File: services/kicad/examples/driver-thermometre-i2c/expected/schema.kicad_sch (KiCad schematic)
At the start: 10 parts, among them J1 CONN_5V_GND_SDA_SCL, U1 AMS1117-3.3

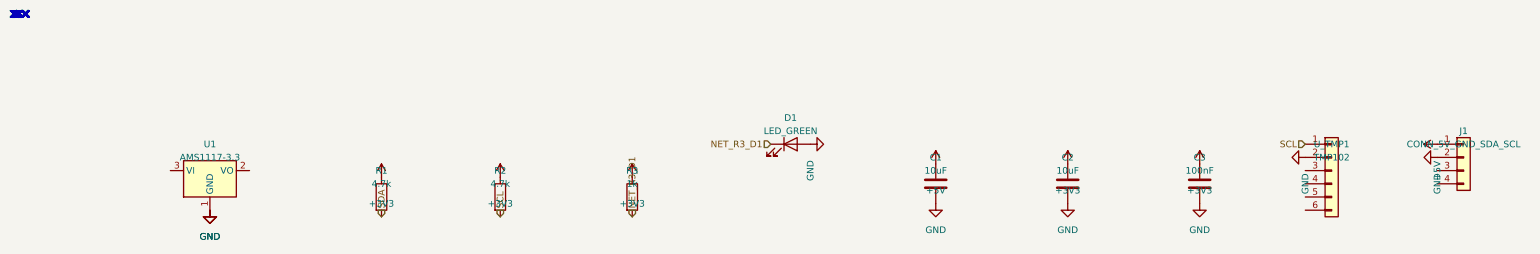
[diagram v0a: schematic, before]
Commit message: fix(agents): l'enrichissement ne reecrit plus un footprint deja qualifie ; exemple driver-thermometre-i2c sur le contrat durci
`quickLookup('J1', …)` rend un PinHeader 1x02 pour tout connecteur, quel que
soit l'indice : un footprint complet et juste (PinHeader_1x04) etait reecrit
en 1x02 dans l'etat publie et la BOM — le board, lui, gardait le bon. Un
footprint `Lib:Nom` ne se cherche plus.

Meme phrase rejouee sur le contrat durci (run 537dc8a5) : SDA passe de 1 a
3 broches, SCL de 2 a 3, 100 % route, 0 erreur, 198 s. README avant/apres.

Co-Authored-By: Claude Fable 5.1 <noreply@anthropic.com>
Claude-Session: https://claude.ai/code/session_01TnMqm4La2CxQHHB5K8aSSV
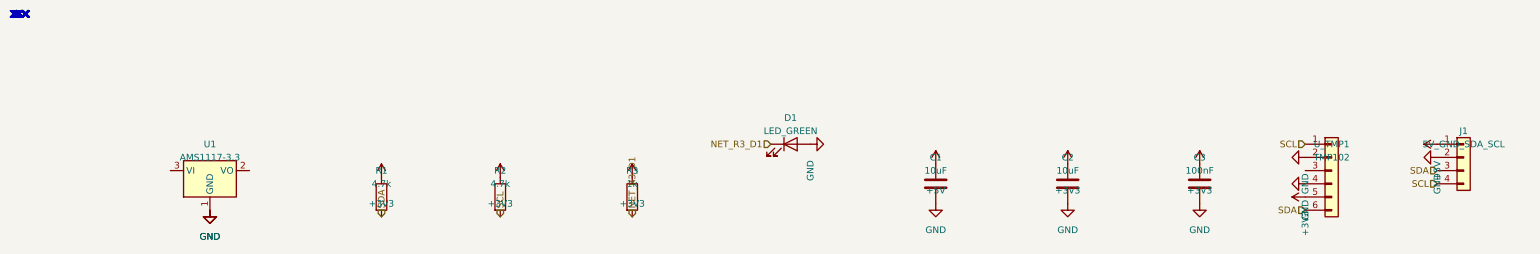
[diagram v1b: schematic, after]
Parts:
- J1: value CONN_5V_GND_SDA_SCL -> 5V_GND_SDA_SCL
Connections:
- net +3V3: now also U_TMP1.5 (Pin_5)
- net GND: now also U_TMP1.4 (Pin_4)
- net SCL: now also J1.4 (Pin_4)
- net SDA: now also J1.3 (Pin_3), U_TMP1.6 (Pin_6)
- no-connect marks 39 -> 33
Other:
- title: 2be02059-834b-4858-8c30-65f833ef493a -> 27ced4b4-4904-46c2-9a70-1466fee604bc
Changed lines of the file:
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@@
 	(paper "A4")
 	(title_block
-		(title "2be02059-834b-4858-8c30-65f833ef493a")
+		(title "27ced4b4-4904-46c2-9a70-1466fee604bc")
 		(date "")
 		(rev "")
@@
 			)
 		)
-		(property "Value" "CONN_5V_GND_SDA_SCL"
+		(property "Value" "5V_GND_SDA_SCL"
 			(at 279.4 25.4 0)
 			(effects
@@
 		(instances
 			(project "project"
-				(path "/40d6248a-0bee-4247-bdab-fa8b0e9ebeb3" (reference "J1") (unit 1)
+				(path "/6469032a-9a26-486a-b3b8-bd033d9a65b8" (reference "J1") (unit 1)
 				)
 			)
@@
 		(instances
 			(project "project"
-				(path "/40d6248a-0bee-4247-bdab-fa8b0e9ebeb3" (reference "U1") (unit 1)
+				(path "/6469032a-9a26-486a-b3b8-bd033d9a65b8" (reference "U1") (unit 1)
 				)
 			)
@@
 		(instances
 			(project "project"
-				(path "/40d6248a-0bee-4247-bdab-fa8b0e9ebeb3" (reference "C1") (unit 1)
+				(path "/6469032a-9a26-486a-b3b8-bd033d9a65b8" (reference "C1") (unit 1)
 				)
 			)
@@
 		(instances
 			(project "project"
-				(path "/40d6248a-0bee-4247-bdab-fa8b0e9ebeb3" (reference "C2") (unit 1)
+				(path "/6469032a-9a26-486a-b3b8-bd033d9a65b8" (reference "C2") (unit 1)
 				)
 			)
@@
 		(instances
 			(project "project"
-				(path "/40d6248a-0bee-4247-bdab-fa8b0e9ebeb3" (reference "C3") (unit 1)
+				(path "/6469032a-9a26-486a-b3b8-bd033d9a65b8" (reference "C3") (unit 1)
 				)
 			)
@@
 		(instances
 			(project "project"
-				(path "/40d6248a-0bee-4247-bdab-fa8b0e9ebeb3" (reference "U_TMP1") (unit 1)
+				(path "/6469032a-9a26-486a-b3b8-bd033d9a65b8" (reference "U_TMP1") (unit 1)
 				)
 			)
@@
 		(instances
 			(project "project"
-				(path "/40d6248a-0bee-4247-bdab-fa8b0e9ebeb3" (reference "R1") (unit 1)
+				(path "/6469032a-9a26-486a-b3b8-bd033d9a65b8" (reference "R1") (unit 1)
 				)
 			)
@@
 		(instances
 			(project "project"
-				(path "/40d6248a-0bee-4247-bdab-fa8b0e9ebeb3" (reference "R2") (unit 1)
+				(path "/6469032a-9a26-486a-b3b8-bd033d9a65b8" (reference "R2") (unit 1)
 				)
 			)
@@
 		(instances
 			(project "project"
-				(path "/40d6248a-0bee-4247-bdab-fa8b0e9ebeb3" (reference "R3") (unit 1)
+				(path "/6469032a-9a26-486a-b3b8-bd033d9a65b8" (reference "R3") (unit 1)
 				)
 			)
@@
 		(instances
 			(project "project"
-				(path "/40d6248a-0bee-4247-bdab-fa8b0e9ebeb3" (reference "D1") (unit 1)
+				(path "/6469032a-9a26-486a-b3b8-bd033d9a65b8" (reference "D1") (unit 1)
 				)
 			)
@@
 		(instances
 			(project "project"
-				(path "/40d6248a-0bee-4247-bdab-fa8b0e9ebeb3" (reference "#PWR001") (unit 1)
+				(path "/6469032a-9a26-486a-b3b8-bd033d9a65b8" (reference "#PWR001") (unit 1)
 				)
 			)
@@
 		(instances
 			(project "project"
-				(path "/40d6248a-0bee-4247-bdab-fa8b0e9ebeb3" (reference "#PWR002") (unit 1)
+				(path "/6469032a-9a26-486a-b3b8-bd033d9a65b8" (reference "#PWR002") (unit 1)
 				)
 			)
@@
 		(instances
 			(project "project"
-				(path "/40d6248a-0bee-4247-bdab-fa8b0e9ebeb3" (reference "#PWR003") (unit 1)
+				(path "/6469032a-9a26-486a-b3b8-bd033d9a65b8" (reference "#PWR003") (unit 1)
 				)
 			)
@@
 		(instances
 			(project "project"
-				(path "/40d6248a-0bee-4247-bdab-fa8b0e9ebeb3" (reference "#PWR004") (unit 1)
+				(path "/6469032a-9a26-486a-b3b8-bd033d9a65b8" (reference "#PWR004") (unit 1)
 				)
 			)
@@
 		(instances
 			(project "project"
-				(path "/40d6248a-0bee-4247-bdab-fa8b0e9ebeb3" (reference "#PWR005") (unit 1)
+				(path "/6469032a-9a26-486a-b3b8-bd033d9a65b8" (reference "#PWR005") (unit 1)
 				)
 			)
@@
 		(instances
 			(project "project"
-				(path "/40d6248a-0bee-4247-bdab-fa8b0e9ebeb3" (reference "#PWR006") (unit 1)
+				(path "/6469032a-9a26-486a-b3b8-bd033d9a65b8" (reference "#PWR006") (unit 1)
 				)
 			)
@@
 		(instances
 			(project "project"
-				(path "/40d6248a-0bee-4247-bdab-fa8b0e9ebeb3" (reference "#PWR007") (unit 1)
+				(path "/6469032a-9a26-486a-b3b8-bd033d9a65b8" (reference "#PWR007") (unit 1)
 				)
 			)
@@
 		(instances
 			(project "project"
-				(path "/40d6248a-0bee-4247-bdab-fa8b0e9ebeb3" (reference "#PWR008") (unit 1)
+				(path "/6469032a-9a26-486a-b3b8-bd033d9a65b8" (reference "#PWR008") (unit 1)
 				)
 			)
@@
 		(instances
 			(project "project"
-				(path "/40d6248a-0bee-4247-bdab-fa8b0e9ebeb3" (reference "#PWR009") (unit 1)
+				(path "/6469032a-9a26-486a-b3b8-bd033d9a65b8" (reference "#PWR009") (unit 1)
+				)
+			)
+		)
+	)
+	(symbol
+		(lib_id "power:GND")
+		(at 248.92 33.02 270)
+		(unit 1)
+		(exclude_from_sim no)
+		(in_bom yes)
+		(on_board yes)
+		(dnp no)
+		(property "Reference" "#PWR010"
+			(at 248.92 35.56 0)
+			(effects
+				(font
+					(size 1.27 1.27)
+				)
+				(hide yes)
+			)
+		)
+		(property "Value" "GND"
+			(at 248.92 38.1 0)
+			(effects
+				(font
+					(size 1.27 1.27)
+				)
+			)
+		)
+		(property "Footprint" ""
+			(at 248.92 33.02 0)
+			(effects
+				(font
+					(size 1.27 1.27)
+				)
+				(hide yes)
+			)
+		)
+		(property "Datasheet" ""
+			(at 248.92 33.02 0)
+			(effects
+				(font
+					(size 1.27 1.27)
+				)
+				(hide yes)
+			)
+		)
+		(pin "1"
+		)
+		(instances
+			(project "project"
+				(path "/6469032a-9a26-486a-b3b8-bd033d9a65b8" (reference "#PWR010") (unit 1)
 				)
 			)
@@
 		(on_board yes)
 		(dnp no)
-		(property "Reference" "#PWR010"
+		(property "Reference" "#PWR011"
 			(at 153.67 27.94 0)
 			(effects
@@
 		(instances
 			(project "project"
-				(path "/40d6248a-0bee-4247-bdab-fa8b0e9ebeb3" (reference "#PWR010") (unit 1)
+				(path "/6469032a-9a26-486a-b3b8-bd033d9a65b8" (reference "#PWR011") (unit 1)
 				)
 			)
@@
 		(on_board yes)
 		(dnp no)
-		(property "Reference" "#PWR011"
+		(property "Reference" "#PWR012"
 			(at 203.2 31.75 0)
 			(effects
@@
 		(instances
 			(project "project"
-				(path "/40d6248a-0bee-4247-bdab-fa8b0e9ebeb3" (reference "#PWR011") (unit 1)
+				(path "/6469032a-9a26-486a-b3b8-bd033d9a65b8" (reference "#PWR012") (unit 1)
 				)
 			)
@@
 		(on_board yes)
 		(dnp no)
-		(property "Reference" "#PWR012"
+		(property "Reference" "#PWR013"
 			(at 228.6 31.75 0)
 			(effects
@@
 		(instances
 			(project "project"
-				(path "/40d6248a-0bee-4247-bdab-fa8b0e9ebeb3" (reference "#PWR012") (unit 1)
+				(path "/6469032a-9a26-486a-b3b8-bd033d9a65b8" (reference "#PWR013") (unit 1)
+				)
+			)
+		)
+	)
+	(symbol
+		(lib_id "power:+3V3")
+		(at 248.92 35.56 90)
+		(unit 1)
+		(exclude_from_sim no)
+		(in_bom yes)
+		(on_board yes)
+		(dnp no)
+		(property "Reference" "#PWR014"
+			(at 248.92 38.1 0)
+			(effects
+				(font
+					(size 1.27 1.27)
+				)
+				(hide yes)
+			)
+		)
+		(property "Value" "+3V3"
+			(at 248.92 40.64 0)
+			(effects
+				(font
+					(size 1.27 1.27)
+				)
+			)
+		)
+		(property "Footprint" ""
+			(at 248.92 35.56 0)
+			(effects
+				(font
+					(size 1.27 1.27)
+				)
+				(hide yes)
+			)
+		)
+		(property "Datasheet" ""
+			(at 248.92 35.56 0)
+			(effects
+				(font
+					(size 1.27 1.27)
+				)
+				(hide yes)
+			)
+		)
+		(pin "1"
+		)
+		(instances
+			(project "project"
+				(path "/6469032a-9a26-486a-b3b8-bd033d9a65b8" (reference "#PWR014") (unit 1)
 				)
 			)
@@
 		(on_board yes)
 		(dnp no)
-		(property "Reference" "#PWR013"
+		(property "Reference" "#PWR015"
 			(at 71.12 34.29 0)
 			(effects
@@
 		(instances
 			(project "project"
-				(path "/40d6248a-0bee-4247-bdab-fa8b0e9ebeb3" (reference "#PWR013") (unit 1)
+				(path "/6469032a-9a26-486a-b3b8-bd033d9a65b8" (reference "#PWR015") (unit 1)
 				)
 			)
@@
 		(on_board yes)
 		(dnp no)
-		(property "Reference" "#PWR014"
+		(property "Reference" "#PWR016"
 			(at 93.98 34.29 0)
 			(effects
@@
 		(instances
 			(project "project"
-				(path "/40d6248a-0bee-4247-bdab-fa8b0e9ebeb3" (reference "#PWR014") (unit 1)
+				(path "/6469032a-9a26-486a-b3b8-bd033d9a65b8" (reference "#PWR016") (unit 1)
 				)
 			)
@@
 		(on_board yes)
 		(dnp no)
-		(property "Reference" "#PWR015"
+		(property "Reference" "#PWR017"
 			(at 119.38 34.29 0)
 			(effects
@@
 		(instances
 			(project "project"
-				(path "/40d6248a-0bee-4247-bdab-fa8b0e9ebeb3" (reference "#PWR015") (unit 1)
-				)
-			)
+				(path "/6469032a-9a26-486a-b3b8-bd033d9a65b8" (reference "#PWR017") (unit 1)
+				)
+			)
+		)
+	)
+	(hierarchical_label "SDA"
+		(shape input)
+		(at 274.32 30.48 180)
+		(fields_autoplaced yes)
+		(effects
+			(font
+				(size 1.27 1.27)
+			)
+			(justify right)
+		)
+	)
+	(hierarchical_label "SDA"
+		(shape input)
+		(at 248.92 38.1 180)
+		(fields_autoplaced yes)
+		(effects
+			(font
+				(size 1.27 1.27)
+			)
+			(justify right)
+		)
+	)
+	(hierarchical_label "SDA"
+		(shape input)
+		(at 71.12 39.37 270)
+		(fields_autoplaced yes)
+		(effects
+			(font
+				(size 1.27 1.27)
+			)
+			(justify left)
+		)
+	)
+	(hierarchical_label "SCL"
+		(shape input)
+		(at 274.32 33.02 180)
+		(fields_autoplaced yes)
+		(effects
+			(font
+				(size 1.27 1.27)
+			)
+			(justify right)
 		)
 	)
@@
 		)
 	)
-	(hierarchical_label "SDA"
-		(shape input)
-		(at 71.12 39.37 270)
-		(fields_autoplaced yes)
-		(effects
-			(font
-				(size 1.27 1.27)
-			)
-			(justify left)
-		)
-	)
 	(hierarchical_label "NET_R3_D1"
 		(shape input)
@@
 	)
 	(sheet_instances
-		(path "/40d6248a-0bee-4247-bdab-fa8b0e9ebeb3" (page "1")
+		(path "/6469032a-9a26-486a-b3b8-bd033d9a65b8" (page "1")
 		)
 	)
@@
   (no_connect (at 2.4892 0.254))
   (no_connect (at 2.4892 0.3048))
-  (no_connect (at 2.4892 0.3302))
-  (no_connect (at 2.4892 0.3556))
   (no_connect (at 2.4892 0.381))
   (no_connect (at 2.7432 0.3048))
@@
   (no_connect (at 2.4892 0.254))
   (no_connect (at 2.4892 0.3048))
-  (no_connect (at 2.4892 0.3302))
-  (no_connect (at 2.4892 0.3556))
   (no_connect (at 2.4892 0.381))
   (no_connect (at 2.7432 0.3048))
@@
   (no_connect (at 2.4892 0.254))
   (no_connect (at 2.4892 0.3048))
-  (no_connect (at 2.4892 0.3302))
-  (no_connect (at 2.4892 0.3556))
   (no_connect (at 2.4892 0.381))
   (no_connect (at 2.7432 0.3048))
